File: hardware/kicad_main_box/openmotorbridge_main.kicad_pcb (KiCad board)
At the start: 4 copper layers, 85 x 55 mm, 14 parts, among them J1 HD26_FEMALE, J2 MicroSD_4Bit_SDIO, J3 USB_C_IP67, U1 LM5164-Q1, U2 ESP32-S3-WROOM-1, U3 ES8388, U4 B0505S-1WR3, U5 BMI270, U6 TCAN334G

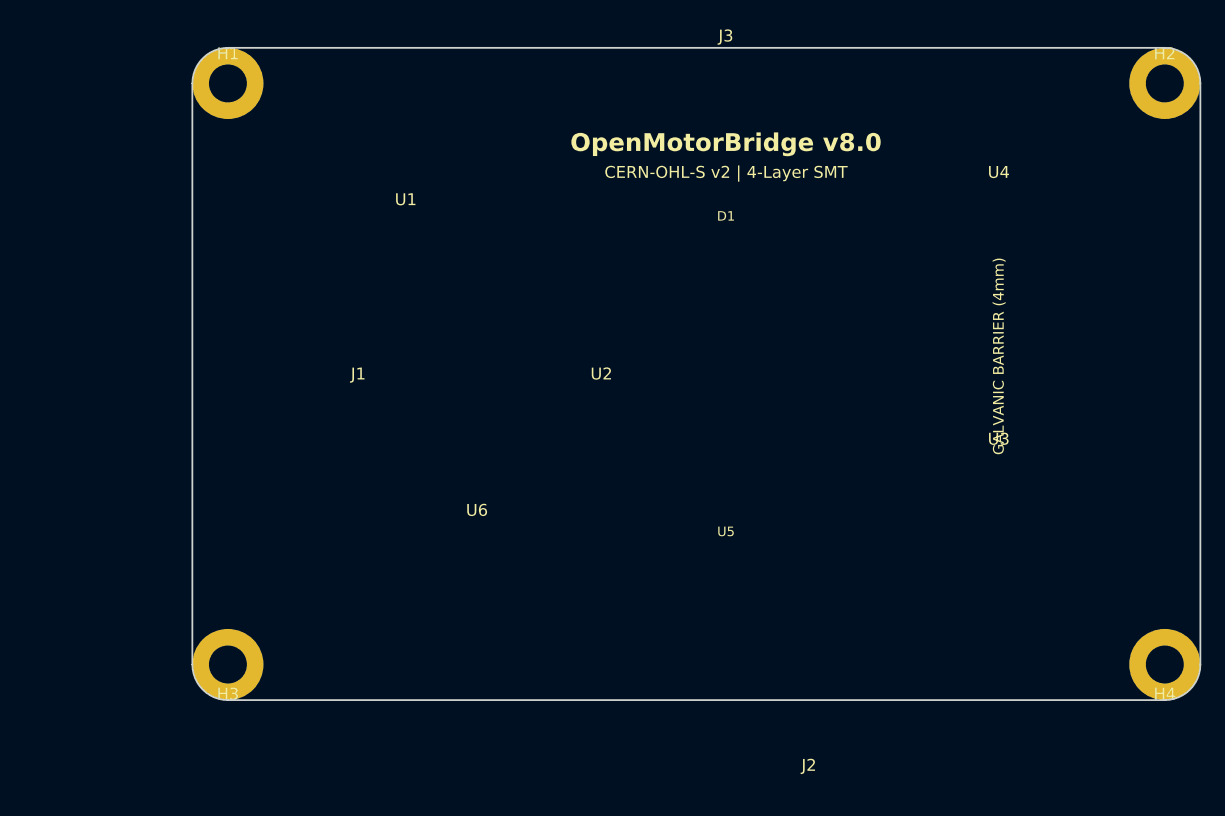
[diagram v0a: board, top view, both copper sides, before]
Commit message: fix(pcb): Center HD26 connector on bottom edge and move MicroSD slot to internal IP67 position
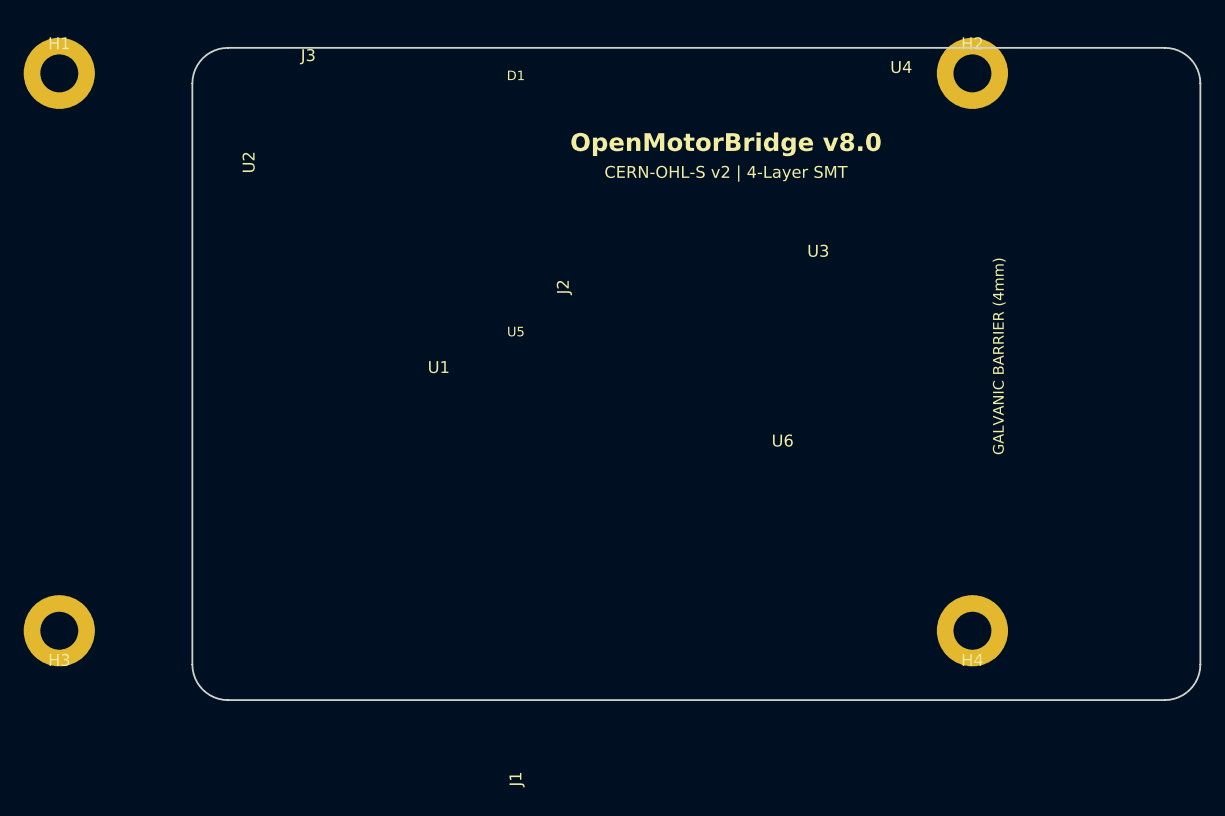
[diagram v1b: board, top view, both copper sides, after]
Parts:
- moved U2 40.9 mm to (120.0, 92.0), turned to 0 degrees
- moved J3 35.3 mm to (125.0, 76.0)
- moved J2 34.1 mm to (155.0, 92.0), turned to 90 degrees
- moved J1 33.6 mm to (142.5, 121.5), turned to 180 degrees
- moved U6 26.4 mm to (165.0, 108.0)
- moved U5 24.5 mm to (142.5, 98.0)
- moved U3 22.0 mm to (168.0, 92.0)
- moved D1 21.3 mm to (142.5, 76.0)
- moved H4 16.5 mm to (181.0, 121.0)
- moved H2 16.2 mm to (181.0, 74.0)
- moved H3 14.5 mm to (104.0, 121.0)
- moved U1 14.4 mm to (136.0, 102.0)
- moved H1 14.2 mm to (104.0, 74.0)
- moved U4 12.1 mm to (175.0, 78.0)
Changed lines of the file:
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@@
 	(footprint "MountingHole:MountingHole_3.2mm_M3_Pad_Via"
 		(layer "F.Cu")
-		(at 118.220238 74.84825)
+		(at 104 74)
 		(property "Reference" "H1"
 			(at 0 -2.5 0)
@@
 	(footprint "MountingHole:MountingHole_3.2mm_M3_Pad_Via"
 		(layer "F.Cu")
-		(at 118.220238 123.84825)
+		(at 104 121)
 		(property "Reference" "H3"
 			(at 0 2.5 0)
@@
 	(footprint "Package_SO:SOIC-8_3.9x4.9mm_P1.27mm"
 		(layer "F.Cu")
-		(at 139.220238 113.84825)
+		(at 165 108)
 		(property "Reference" "U6"
 			(at 0 -3 0)
@@
 	(footprint "MountingHole:MountingHole_3.2mm_M3_Pad_Via"
 		(layer "F.Cu")
-		(at 197.220238 123.84825)
+		(at 181 121)
 		(property "Reference" "H4"
 			(at 0 2.5 0)
@@
 	(footprint "RF_Module:ESP32-S3-WROOM-1"
 		(layer "F.Cu")
-		(at 160.220238 99.34825 90)
+		(at 120 92)
 		(property "Reference" "U2"
-			(at 0 -10.5 0)
+			(at 0 -10.5 270)
 			(layer "F.SilkS")
 			(effects
@@
 		)
 		(property "Value" "ESP32-S3-WROOM-1"
-			(at 0 10.5 0)
-			(layer "F.Fab")
-			(effects
-				(font
-					(size 1 1)
-					(thickness 0.15)
-				)
-			)
-		)
-		(property "Datasheet" ""
-			(at 0 0 90)
-			(layer "F.Fab")
-			(hide yes)
-			(effects
-				(font
-					(size 1.27 1.27)
-				)
-			)
-		)
-		(property "Description" ""
-			(at 0 0 90)
+			(at 0 10.5 270)
+			(layer "F.Fab")
+			(effects
+				(font
+					(size 1 1)
+					(thickness 0.15)
+				)
+			)
+		)
+		(property "Datasheet" ""
+			(at 0 0 0)
+			(layer "F.Fab")
+			(hide yes)
+			(effects
+				(font
+					(size 1.27 1.27)
+				)
+			)
+		)
+		(property "Description" ""
+			(at 0 0 0)
 			(layer "F.Fab")
 			(hide yes)
@@
 	(footprint "Connector_USB:USB_C_Receptacle_GCT_USB4085"
 		(layer "F.Cu")
-		(at 160.220238 74.34825)
+		(at 125 76)
 		(property "Reference" "J3"
 			(at 0 -3.5 0)
@@
 	(footprint "Package_LGA:LGA-14_2.5x3mm_P0.5mm"
 		(layer "F.Cu")
-		(at 160.220238 114.84825)
+		(at 142.5 98)
 		(property "Reference" "U5"
 			(at 0 -2.2 0)
@@
 	(footprint "Connector_Card:microSD_HC_Molex_47571-0001"
 		(layer "F.Cu")
-		(at 167.220238 123.84825 180)
+		(at 155 92 90)
 		(property "Reference" "J2"
-			(at 0 -8.5 0)
+			(at 0 -8.5 270)
 			(layer "F.SilkS")
 			(effects
@@
 		)
 		(property "Value" "MicroSD_4Bit_SDIO"
-			(at 0 8.5 0)
-			(layer "F.Fab")
-			(effects
-				(font
-					(size 1 1)
-					(thickness 0.15)
-				)
-			)
-		)
-		(property "Datasheet" ""
-			(at 0 0 180)
-			(layer "F.Fab")
-			(hide yes)
-			(effects
-				(font
-					(size 1.27 1.27)
-				)
-			)
-		)
-		(property "Description" ""
-			(at 0 0 180)
+			(at 0 8.5 270)
+			(layer "F.Fab")
+			(effects
+				(font
+					(size 1 1)
+					(thickness 0.15)
+				)
+			)
+		)
+		(property "Datasheet" ""
+			(at 0 0 90)
+			(layer "F.Fab")
+			(hide yes)
+			(effects
+				(font
+					(size 1.27 1.27)
+				)
+			)
+		)
+		(property "Description" ""
+			(at 0 0 90)
 			(layer "F.Fab")
 			(hide yes)
@@
 	(footprint "LED_SMD:LED_WS2812B-2020"
 		(layer "F.Cu")
-		(at 160.220238 87.84825)
+		(at 142.5 76)
 		(property "Reference" "D1"
 			(at 0 -1.8 0)
@@
 	(footprint "Connector_Dsub:DSUB-26-HD_Female_Horizontal_P2.29x1.98mm_EdgePinOffset7.70mm_Housings_POS01"
 		(layer "F.Cu")
-		(at 117.220238 99.34825 -90)
+		(at 142.5 121.5 180)
 		(property "Reference" "J1"
-			(at 0 -12 0)
+			(at 0 -12 270)
 			(layer "F.SilkS")
 			(effects
@@
 		)
 		(property "Value" "HD26_FEMALE"
-			(at 0 12 0)
-			(layer "F.Fab")
-			(effects
-				(font
-					(size 1 1)
-					(thickness 0.15)
-				)
-			)
-		)
-		(property "Datasheet" ""
-			(at 0 0 270)
-			(layer "F.Fab")
-			(hide yes)
-			(effects
-				(font
-					(size 1.27 1.27)
-				)
-			)
-		)
-		(property "Description" ""
-			(at 0 0 270)
+			(at 0 12 270)
+			(layer "F.Fab")
+			(effects
+				(font
+					(size 1 1)
+					(thickness 0.15)
+				)
+			)
+		)
+		(property "Datasheet" ""
+			(at 0 0 180)
+			(layer "F.Fab")
+			(hide yes)
+			(effects
+				(font
+					(size 1.27 1.27)
+				)
+			)
+		)
+		(property "Description" ""
+			(at 0 0 180)
 			(layer "F.Fab")
 			(hide yes)
@@
 	(footprint "Package_SO:SOIC-8-1EP_3.9x4.9mm_P1.27mm_EP2.41x3.3mm"
 		(layer "F.Cu")
-		(at 133.220238 87.84825)
+		(at 136 102)
 		(property "Reference" "U1"
 			(at 0 -3.2 0)
@@
 	(footprint "Converter_DCDC:Converter_DCDC_Mornsun_B_S-1WR3_THT"
 		(layer "F.Cu")
-		(at 183.220238 86.84825)
+		(at 175 78)
 		(property "Reference" "U4"
 			(at 0 -4.5 0)
@@
 	(footprint "MountingHole:MountingHole_3.2mm_M3_Pad_Via"
 		(layer "F.Cu")
-		(at 197.220238 74.84825)
+		(at 181 74)
 		(property "Reference" "H2"
 			(at 0 -2.5 0)
@@
 	(footprint "Package_DFN_QFN:QFN-28-1EP_4x4mm_P0.4mm_EP2.6x2.6mm"
 		(layer "F.Cu")
-		(at 183.220238 107.84825)
+		(at 168 92)
 		(property "Reference" "U3"
 			(at 0 -3 0)

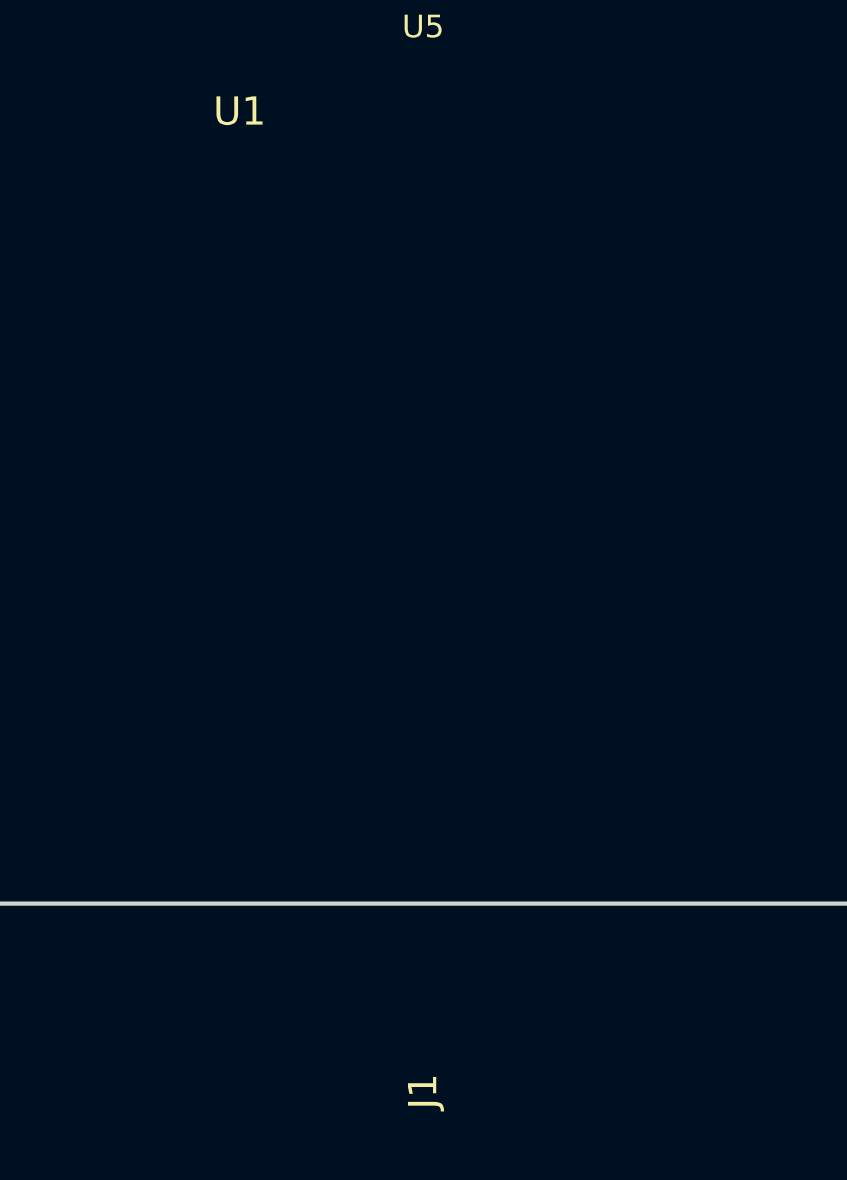
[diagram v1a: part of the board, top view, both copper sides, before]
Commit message: fix(pcb): Replace direct HD26 with 2x13 IDC shrouded box header for ribbon cable chassis connection
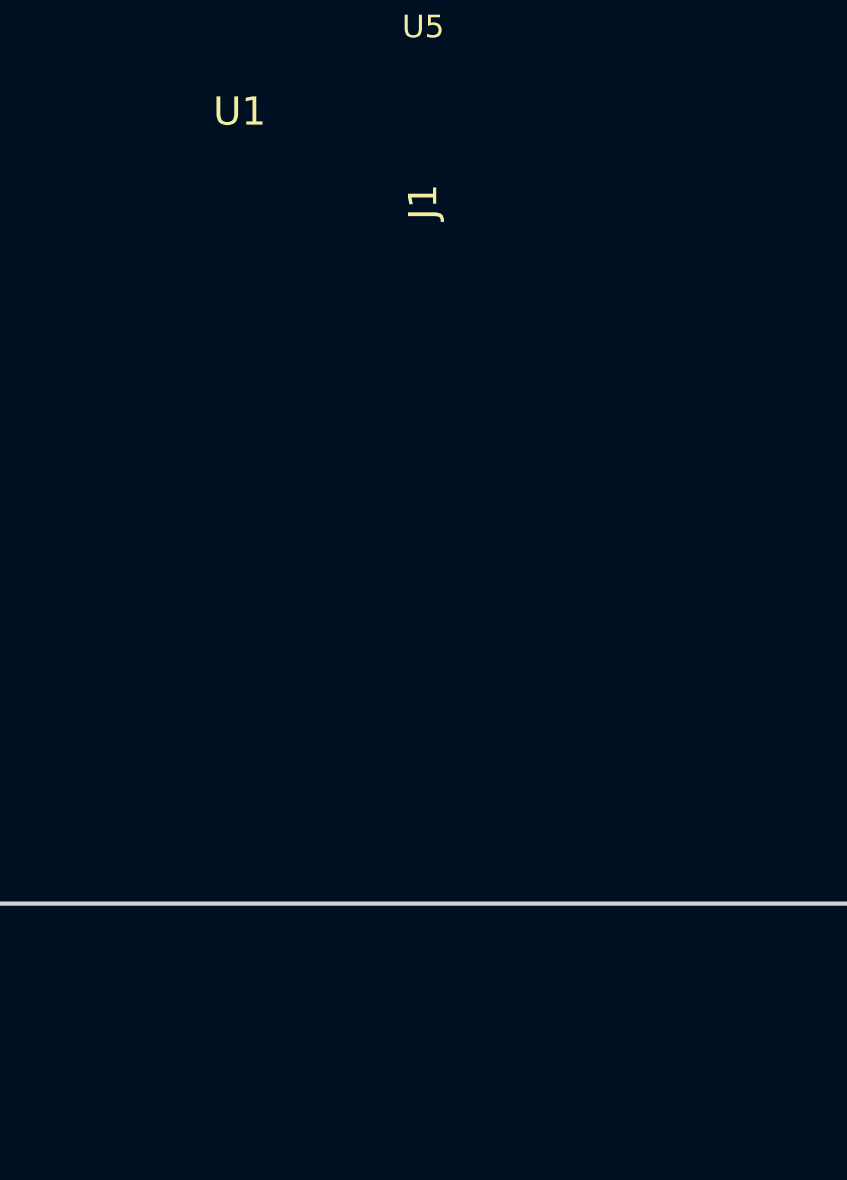
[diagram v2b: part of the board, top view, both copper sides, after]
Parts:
- J1: value HD26_FEMALE -> IDC_2X13_HEADER
- moved J1 7.50 mm to (142.5, 114.0), turned to 0 degrees
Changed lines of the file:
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@@
 	(footprint "Connector_Dsub:DSUB-26-HD_Female_Horizontal_P2.29x1.98mm_EdgePinOffset7.70mm_Housings_POS01"
 		(layer "F.Cu")
-		(at 142.5 121.5 180)
+		(at 142.5 114)
 		(property "Reference" "J1"
-			(at 0 -12 270)
+			(at 0 -12 90)
 			(layer "F.SilkS")
 			(effects
@@
 			)
 		)
-		(property "Value" "HD26_FEMALE"
-			(at 0 12 270)
+		(property "Value" "IDC_2X13_HEADER"
+			(at 0 12 90)
 			(layer "F.Fab")
 			(effects
@@
 		)
 		(property "Datasheet" ""
-			(at 0 0 180)
+			(at 0 0 0)
 			(layer "F.Fab")
 			(hide yes)
@@
 		)
 		(property "Description" ""
-			(at 0 0 180)
+			(at 0 0 0)
 			(layer "F.Fab")
 			(hide yes)
@@
 		(duplicate_pad_numbers_are_jumpers no)
 		(embedded_fonts no)
-		(model "/Connector_Dsub.3dshapes/DSUB-25_Socket_Horizontal_P2.77x2.84mm_EdgePinOffset7.70mm_Housed_MountingHolesOffset9.12mm.step"
+		(model "/Connector_IDC.3dshapes/IDC-Header_2x13_P2.54mm_Vertical.step"
 			(offset
 				(xyz 0 0 0)

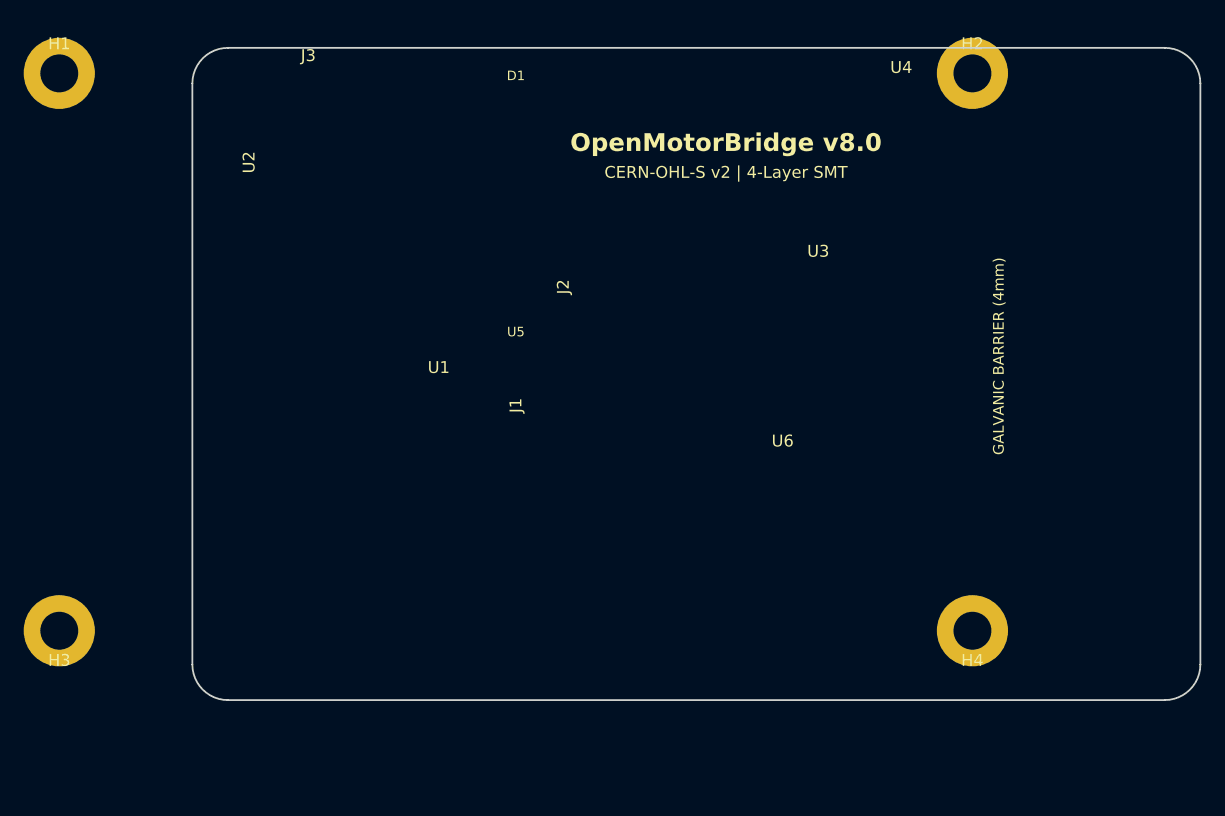
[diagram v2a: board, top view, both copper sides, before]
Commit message: feat(hardware): finalize main box PCB layout with full component matrix and autoplace script
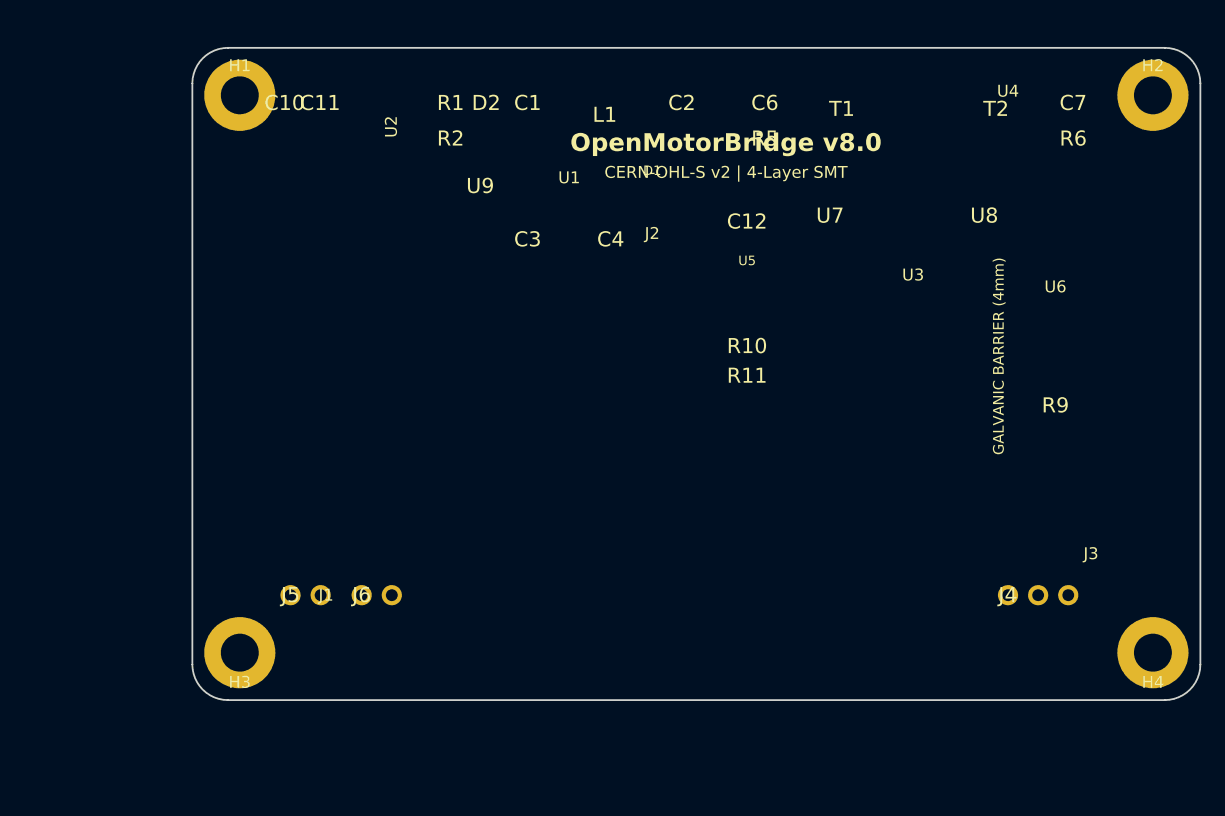
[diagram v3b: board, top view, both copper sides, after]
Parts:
- added C1: 10uF_100V, , F.Cu at (143.5, 76.5)
- added C10: 100nF_MCU, , F.Cu at (123.0, 76.5)
- added C11: 10uF_MCU, , F.Cu at (126.0, 76.5)
- added C12: 100nF_IMU, , F.Cu at (162.0, 86.5)
- added C2: 22uF_16V, , F.Cu at (156.5, 76.5)
- added C3: 100nF, , F.Cu at (143.5, 88.0)
- added C4: 100nF, , F.Cu at (150.5, 88.0)
- added C6: 1uF_Audio, , F.Cu at (163.5, 76.5)
- added C7: 1uF_Audio, , F.Cu at (189.5, 76.5)
- added D2: SMBJ33CA_TVS, , F.Cu at (140.0, 76.5)
- added J4: LED_EXT, , F.Cu at (184.0, 118.0)
- added J5: BAT_LIPO_3V7, , F.Cu at (123.5, 118.0)
- added J6: NTC_10K_JEITA, , F.Cu at (129.5, 118.0)
- added L1: 47uH_PowerInductor, , F.Cu at (150.0, 77.5)
- added R1: 100k_1%, , F.Cu at (137.0, 76.5)
- added R10: 4k7_I2C, , F.Cu at (162.0, 97.0)
- added R11: 4k7_I2C, , F.Cu at (162.0, 99.5)
- added R2: 10k_1%, , F.Cu at (137.0, 79.5)
- added R5: 600R_Term, , F.Cu at (163.5, 79.5)
- added R6: 600R_Term, , F.Cu at (189.5, 79.5)
- added R9: 120R_CAN, , F.Cu at (188.0, 102.0)
- added T1: Bourns_LM-NP-1001_Audio1, , F.Cu at (170.0, 77.0)
- added T2: Bourns_LM-NP-1001_Audio2, , F.Cu at (183.0, 77.0)
- added U7: TLP222A_Opto1, , F.Cu at (169.0, 86.0)
- added U8: TLP222A_Opto2, , F.Cu at (182.0, 86.0)
- added U9: TPS7A0533_LDO, , F.Cu at (139.5, 83.5)
- moved J3 78.2 mm to (191.0, 118.0)
- moved U6 26.4 mm to (188.0, 95.0)
- moved U5 20.4 mm to (162.0, 92.0)
- moved U1 19.4 mm to (147.0, 86.0)
- moved H1 15.3 mm to (119.2, 75.8)
- moved H2 15.3 mm to (196.2, 75.8)
- moved H3 15.3 mm to (119.2, 122.8)
- moved H4 15.3 mm to (196.2, 122.8)
- moved D1 14.0 mm to (154.0, 84.0)
- moved U2 12.4 mm to (132.0, 89.0)
- moved U4 9.22 mm to (184.0, 80.0)
- moved U3 8.25 mm to (176.0, 94.0)
- moved J1 5.66 mm to (138.5, 118.0), turned to 90 degrees
- moved J2 4.12 mm to (154.0, 96.0), turned to 0 degrees
